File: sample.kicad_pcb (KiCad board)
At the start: 2 copper layers, 4 parts, among them J1 Conn_02x08_Odd_Even, J2 Conn_02x15_Odd_Even, J3 Conn_02x10_Odd_Even, J4 Conn_02x17_Odd_Even

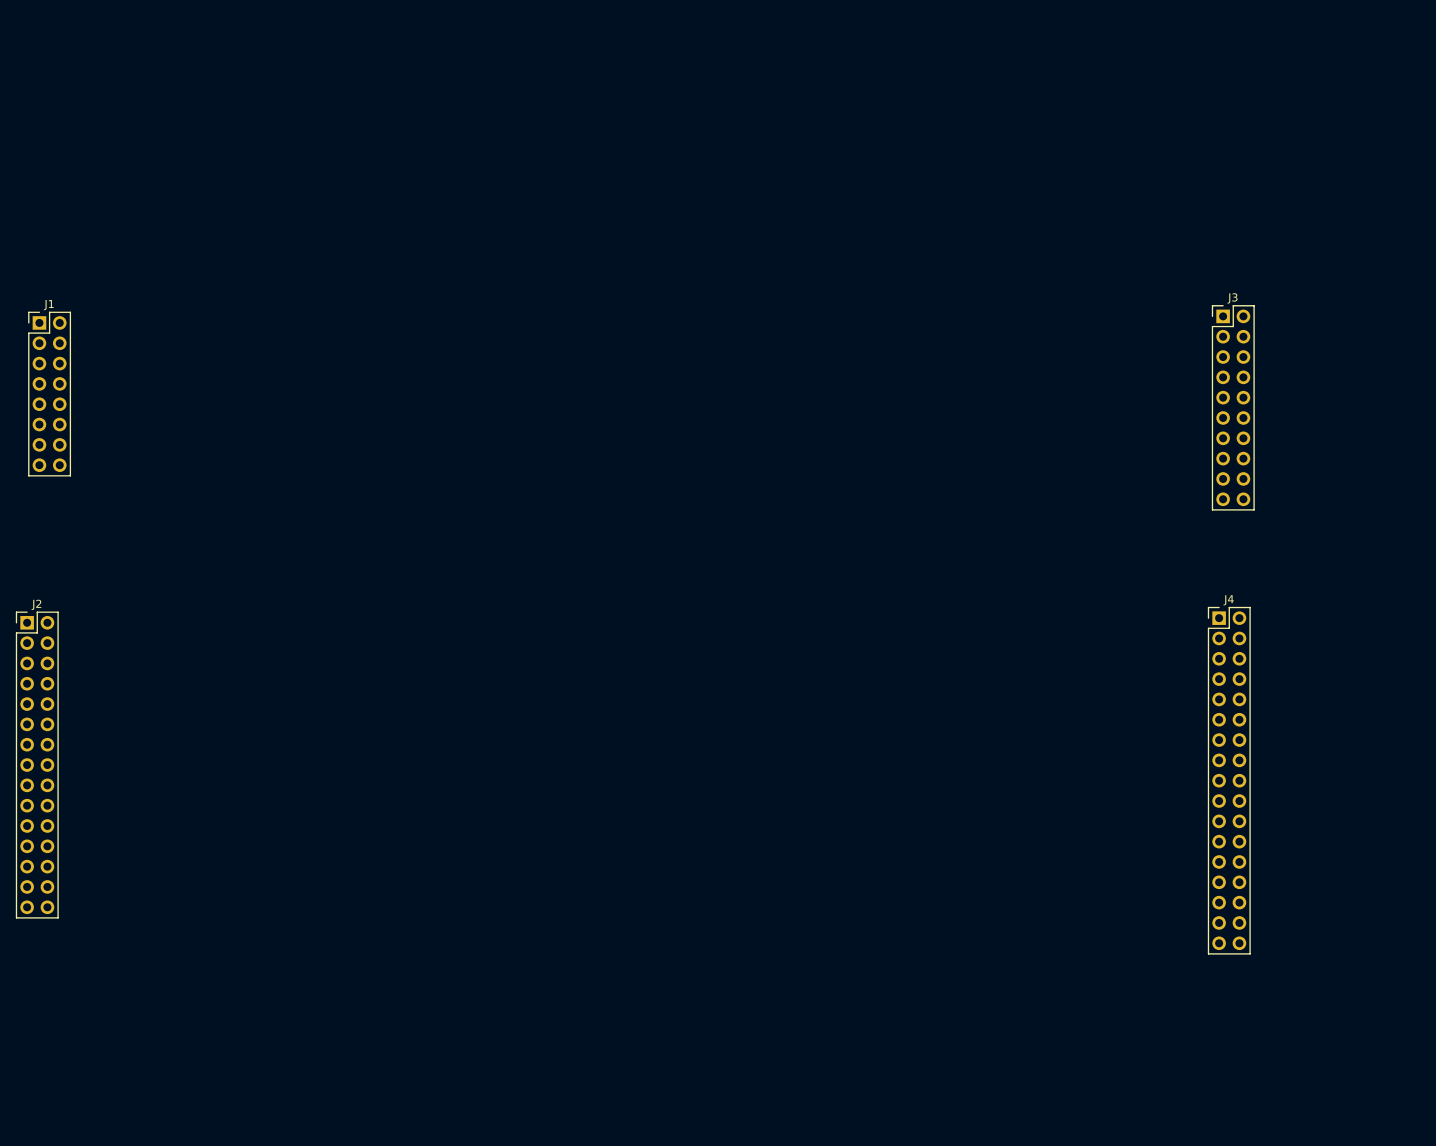
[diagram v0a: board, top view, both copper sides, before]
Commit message: split into hirachical pages
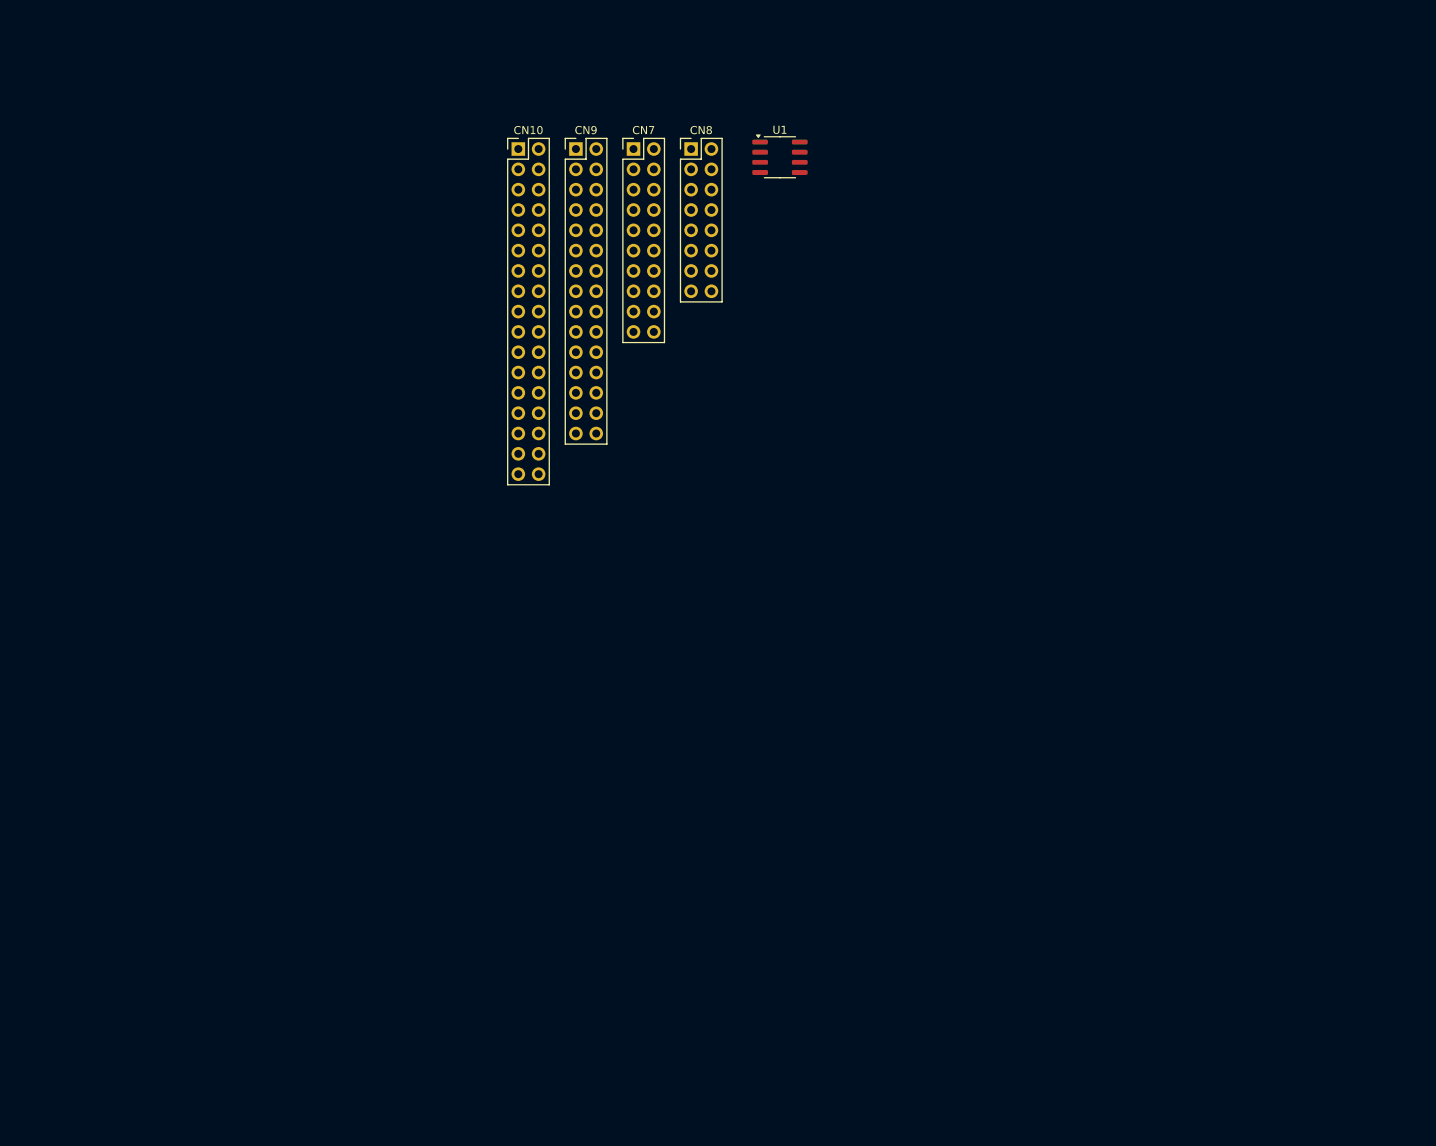
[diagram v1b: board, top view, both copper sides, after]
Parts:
- removed J1: Conn_02x08_Odd_Even, Connector_PinHeader_2.54mm:PinHeader_2x08_P2.54mm_Vertical
- removed J2: Conn_02x15_Odd_Even, Connector_PinHeader_2.54mm:PinHeader_2x15_P2.54mm_Vertical
- removed J3: Conn_02x10_Odd_Even, Connector_PinHeader_2.54mm:PinHeader_2x10_P2.54mm_Vertical
- removed J4: Conn_02x17_Odd_Even, Connector_PinHeader_2.54mm:PinHeader_2x17_P2.54mm_Vertical
- added CN10: Conn_02x17_Odd_Even, Connector_PinHeader_2.54mm:PinHeader_2x17_P2.54mm_Vertical, F.Cu at (124.4, 42.2)
- added CN7: Conn_02x10_Odd_Even, Connector_PinHeader_2.54mm:PinHeader_2x10_P2.54mm_Vertical, F.Cu at (138.8, 42.2)
- added CN8: Conn_02x08_Odd_Even, Connector_PinHeader_2.54mm:PinHeader_2x08_P2.54mm_Vertical, F.Cu at (146.0, 42.2)
- added CN9: Conn_02x15_Odd_Even, Connector_PinHeader_2.54mm:PinHeader_2x15_P2.54mm_Vertical, F.Cu at (131.6, 42.2)
- added U1: TJA1042T-3, Package_SO:SOIC-8_3.9x4.9mm_P1.27mm, F.Cu at (157.1, 43.2)

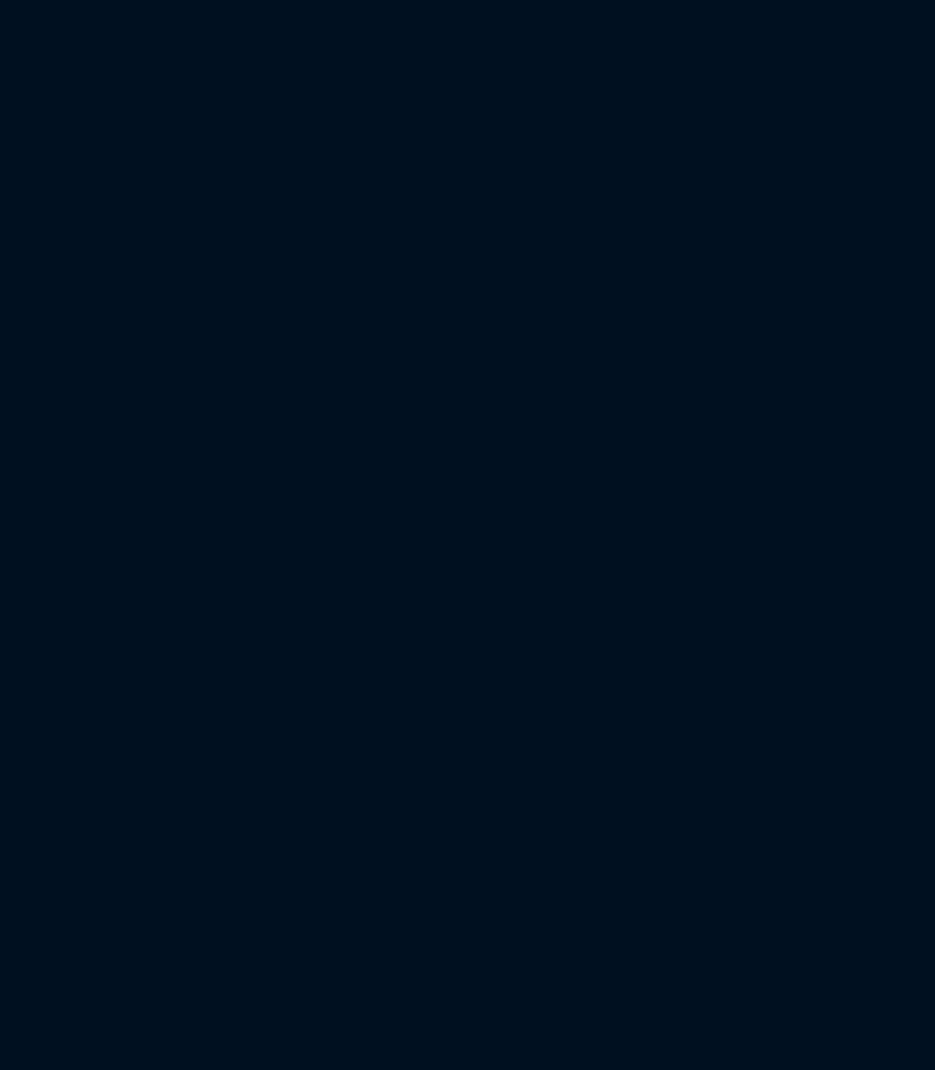
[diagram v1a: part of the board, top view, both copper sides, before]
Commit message: fix double numbers
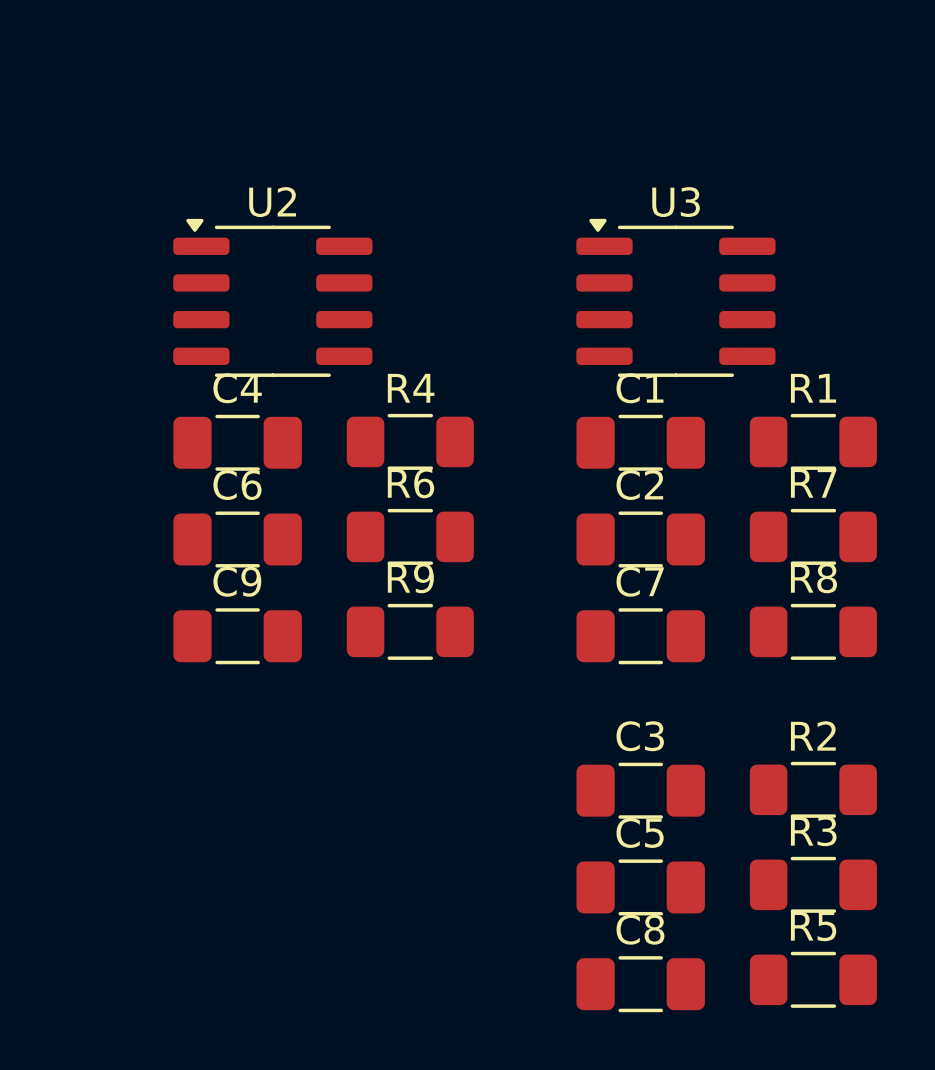
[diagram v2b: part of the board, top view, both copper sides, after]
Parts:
- added C1: 47nF, Capacitor_SMD:C_1206_3216Metric_Pad1.33x1.80mm_HandSolder, F.Cu at (176.0, 71.4)
- added C2: 47nF, Capacitor_SMD:C_1206_3216Metric_Pad1.33x1.80mm_HandSolder, F.Cu at (176.0, 74.8)
- added C3: 47nF, Capacitor_SMD:C_1206_3216Metric_Pad1.33x1.80mm_HandSolder, F.Cu at (176.0, 83.5)
- added C4: 47nF, Capacitor_SMD:C_1206_3216Metric_Pad1.33x1.80mm_HandSolder, F.Cu at (162.0, 71.4)
- added C5: 47nF, Capacitor_SMD:C_1206_3216Metric_Pad1.33x1.80mm_HandSolder, F.Cu at (176.0, 86.8)
- added C6: C, Capacitor_SMD:C_1206_3216Metric_Pad1.33x1.80mm_HandSolder, F.Cu at (162.0, 74.8)
- added C7: C, Capacitor_SMD:C_1206_3216Metric_Pad1.33x1.80mm_HandSolder, F.Cu at (176.0, 78.1)
- added C8: C, Capacitor_SMD:C_1206_3216Metric_Pad1.33x1.80mm_HandSolder, F.Cu at (176.0, 90.2)
- added C9: 47nF, Capacitor_SMD:C_1206_3216Metric_Pad1.33x1.80mm_HandSolder, F.Cu at (162.0, 78.1)
- added R1: R, Resistor_SMD:R_1206_3216Metric_Pad1.30x1.75mm_HandSolder, F.Cu at (181.9, 71.4)
- added R2: R, Resistor_SMD:R_1206_3216Metric_Pad1.30x1.75mm_HandSolder, F.Cu at (181.9, 83.4)
- added R3: R, Resistor_SMD:R_1206_3216Metric_Pad1.30x1.75mm_HandSolder, F.Cu at (181.9, 86.7)
- added R4: R, Resistor_SMD:R_1206_3216Metric_Pad1.30x1.75mm_HandSolder, F.Cu at (168.0, 71.4)
- added R5: R, Resistor_SMD:R_1206_3216Metric_Pad1.30x1.75mm_HandSolder, F.Cu at (181.9, 90.0)
- added R6: R, Resistor_SMD:R_1206_3216Metric_Pad1.30x1.75mm_HandSolder, F.Cu at (168.0, 74.7)
- added R7: R, Resistor_SMD:R_1206_3216Metric_Pad1.30x1.75mm_HandSolder, F.Cu at (181.9, 74.7)
- added R8: R, Resistor_SMD:R_1206_3216Metric_Pad1.30x1.75mm_HandSolder, F.Cu at (181.9, 78.0)
- added R9: R, Resistor_SMD:R_1206_3216Metric_Pad1.30x1.75mm_HandSolder, F.Cu at (168.0, 78.0)
- added U2: TJA1042T-3, Package_SO:SOIC-8_3.9x4.9mm_P1.27mm, F.Cu at (163.2, 66.5)
- added U3: TJA1042T-3, Package_SO:SOIC-8_3.9x4.9mm_P1.27mm, F.Cu at (177.2, 66.5)
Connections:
- U1 pad 6: unconnected-(U1-CANL-Pad6) -> CAN1_L
- U1 pad 7: unconnected-(U1-CANH-Pad7) -> CAN1_H
- U1 pad 8: unconnected-(U1-STB-Pad8) -> CAN1_STB

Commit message: connect CANs to ZIO
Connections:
- CN10 pad 11: /Connectors/PF6 -> CAN3_RX
- CN10 pad 14: /Connectors/PB6 -> CAN2_TX
- CN7 pad 7: /Connectors/PB12 -> CAN2_RX
- CN9 pad 26: /Connectors/PF7 -> CAN3_TX

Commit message: move connectors to zio_connectors
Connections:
- net /Connectors/IOREF renamed /ZIO Connector/IOREF
- net /Connectors/NRST renamed /ZIO Connector/NRST
- net /Connectors/PA0 renamed /ZIO Connector/PA0
- net /Connectors/PA15 renamed /ZIO Connector/PA15
- net /Connectors/PA3 renamed /ZIO Connector/PA3
- net /Connectors/PA4 renamed /ZIO Connector/PA4
- net /Connectors/PA5 renamed /ZIO Connector/PA5
- net /Connectors/PA6 renamed /ZIO Connector/PA6
- net /Connectors/PB0 renamed /ZIO Connector/PB0
- net /Connectors/PB1 renamed /ZIO Connector/PB1
- net /Connectors/PB10 renamed /ZIO Connector/PB10
- net /Connectors/PB11 renamed /ZIO Connector/PB11
- net /Connectors/PB15 renamed /ZIO Connector/PB15
- net /Connectors/PB2 renamed /ZIO Connector/PB2
- net /Connectors/PB3 renamed /ZIO Connector/PB3
- net /Connectors/PB4 renamed /ZIO Connector/PB4
- net /Connectors/PB5 renamed /ZIO Connector/PB5
- net /Connectors/PB7 renamed /ZIO Connector/PB7
- net /Connectors/PB8 renamed /ZIO Connector/PB8
- net /Connectors/PB9 renamed /ZIO Connector/PB9
- net /Connectors/PC0 renamed /ZIO Connector/PC0
- net /Connectors/PC10 renamed /ZIO Connector/PC10
- net /Connectors/PC11 renamed /ZIO Connector/PC11
- net /Connectors/PC12 renamed /ZIO Connector/PC12
- net /Connectors/PC2 renamed /ZIO Connector/PC2
- net /Connectors/PC3 renamed /ZIO Connector/PC3
- net /Connectors/PC6 renamed /ZIO Connector/PC6
- net /Connectors/PC7 renamed /ZIO Connector/PC7
- net /Connectors/PC8 renamed /ZIO Connector/PC8
- net /Connectors/PC9 renamed /ZIO Connector/PC9
- net /Connectors/PD11 renamed /ZIO Connector/PD11
- net /Connectors/PD12 renamed /ZIO Connector/PD12
- net /Connectors/PD13 renamed /ZIO Connector/PD13
- net /Connectors/PD14 renamed /ZIO Connector/PD14
- net /Connectors/PD15 renamed /ZIO Connector/PD15
- net /Connectors/PD2 renamed /ZIO Connector/PD2
- net /Connectors/PD3 renamed /ZIO Connector/PD3
- net /Connectors/PD4 renamed /ZIO Connector/PD4
- net /Connectors/PD5 renamed /ZIO Connector/PD5
- net /Connectors/PD6 renamed /ZIO Connector/PD6
- net /Connectors/PD7 renamed /ZIO Connector/PD7
- net /Connectors/PE0 renamed /ZIO Connector/PE0
- net /Connectors/PE10 renamed /ZIO Connector/PE10
- net /Connectors/PE11 renamed /ZIO Connector/PE11
- net /Connectors/PE12 renamed /ZIO Connector/PE12
- net /Connectors/PE13 renamed /ZIO Connector/PE13
- net /Connectors/PE14 renamed /ZIO Connector/PE14
- net /Connectors/PE15 renamed /ZIO Connector/PE15
- net /Connectors/PE2 renamed /ZIO Connector/PE2
- net /Connectors/PE3 renamed /ZIO Connector/PE3
- net /Connectors/PE4 renamed /ZIO Connector/PE4
- net /Connectors/PE5 renamed /ZIO Connector/PE5
- net /Connectors/PE6 renamed /ZIO Connector/PE6
- net /Connectors/PE7 renamed /ZIO Connector/PE7
- net /Connectors/PE8 renamed /ZIO Connector/PE8
- net /Connectors/PE9 renamed /ZIO Connector/PE9
- net /Connectors/PF0 renamed /ZIO Connector/PF0
- net /Connectors/PF1 renamed /ZIO Connector/PF1
- net /Connectors/PF10 renamed /ZIO Connector/PF10
- net /Connectors/PF2 renamed /ZIO Connector/PF2
- net /Connectors/PF4 renamed /ZIO Connector/PF4
- net /Connectors/PF5 renamed /ZIO Connector/PF5
- net /Connectors/PF8 renamed /ZIO Connector/PF8
- net /Connectors/PF9 renamed /ZIO Connector/PF9
- net /Connectors/PG0 renamed /ZIO Connector/PG0
- net /Connectors/PG1 renamed /ZIO Connector/PG1
- net /Connectors/PG12 renamed /ZIO Connector/PG12
- net /Connectors/PG14 renamed /ZIO Connector/PG14
- net /Connectors/PG2 renamed /ZIO Connector/PG2
- net /Connectors/PG3 renamed /ZIO Connector/PG3
- net /Connectors/PG6 renamed /ZIO Connector/PG6
- net /Connectors/VREFP renamed /ZIO Connector/VREFP

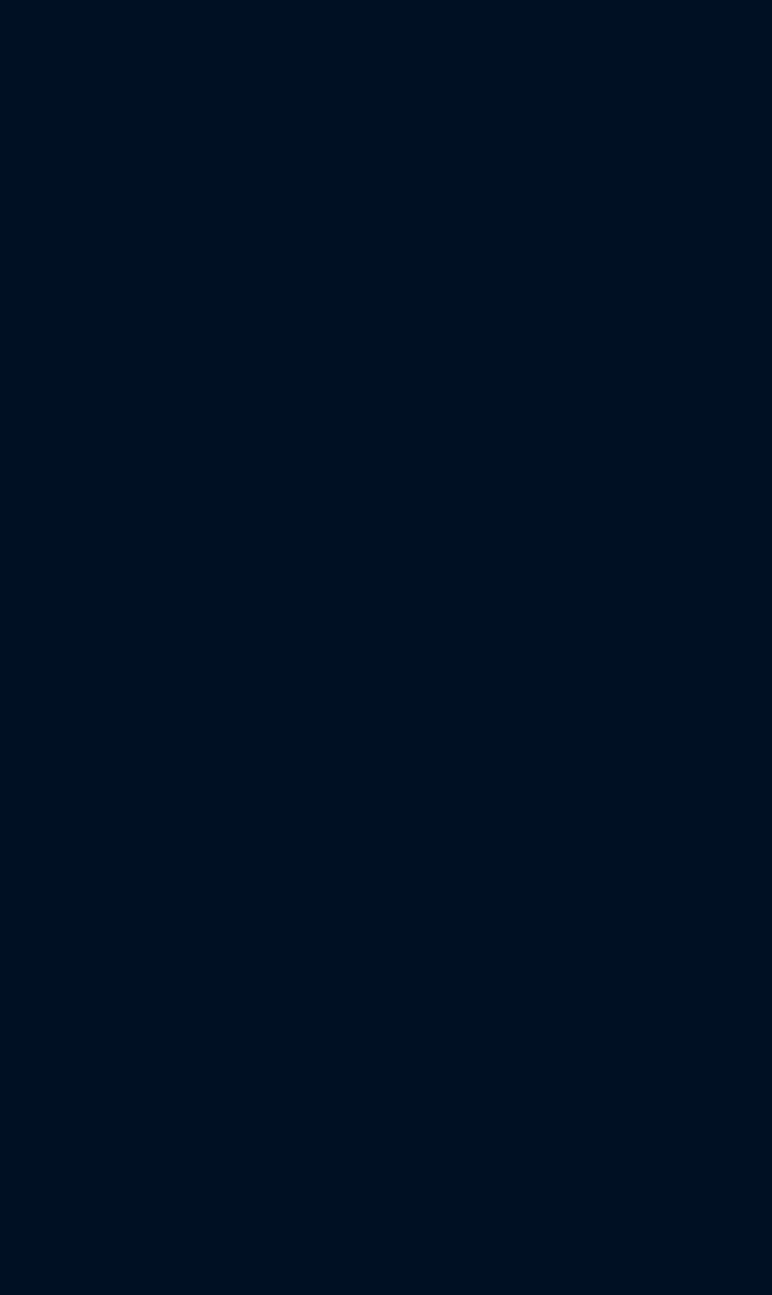
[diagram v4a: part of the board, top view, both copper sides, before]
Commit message: rename jumpers
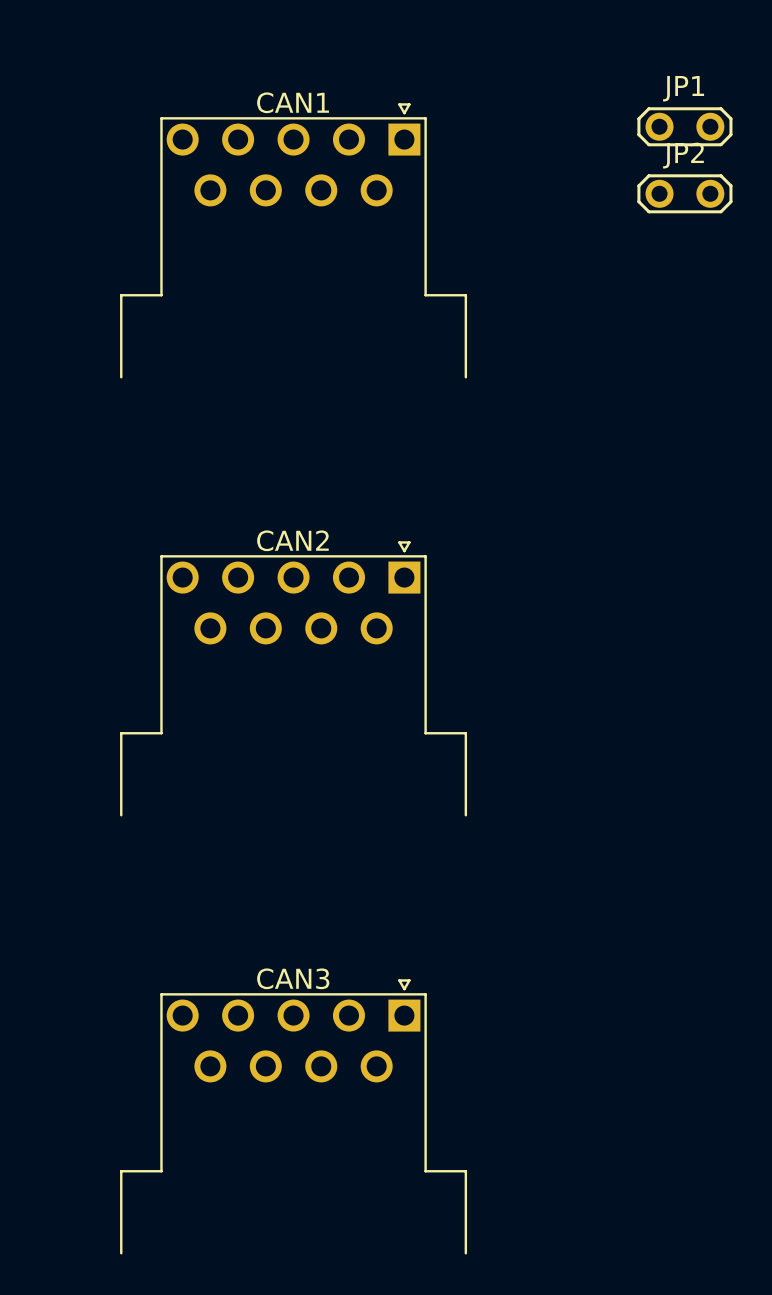
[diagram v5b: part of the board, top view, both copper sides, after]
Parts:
- added CAN1: DE9_Plug, Connector_Dsub:DSUB-9_Female_Horizontal_P2.77x2.54mm_EdgePinOffset9.40mm, F.Cu at (220.7, 43.8)
- added CAN2: DE9_Plug, Connector_Dsub:DSUB-9_Female_Horizontal_P2.77x2.54mm_EdgePinOffset9.40mm, F.Cu at (220.7, 65.7)
- added CAN3: DE9_Plug, Connector_Dsub:DSUB-9_Female_Horizontal_P2.77x2.54mm_EdgePinOffset9.40mm, F.Cu at (220.7, 87.6)
- added JP1: CAN 2 High, TestPoint:TestPoint_2Pads_Pitch2.54mm_Drill0.8mm, F.Cu at (233.5, 43.1)
- added JP2: CAN 2 Low, TestPoint:TestPoint_2Pads_Pitch2.54mm_Drill0.8mm, F.Cu at (233.5, 46.5)
